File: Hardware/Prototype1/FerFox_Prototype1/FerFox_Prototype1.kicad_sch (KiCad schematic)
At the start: 33 parts, among them J1 Conn_01x08_Pin, J2 Conn_01x06_Pin, U1 STM32F401CCUx, Y1 25MHz, Y2 32768 Hz

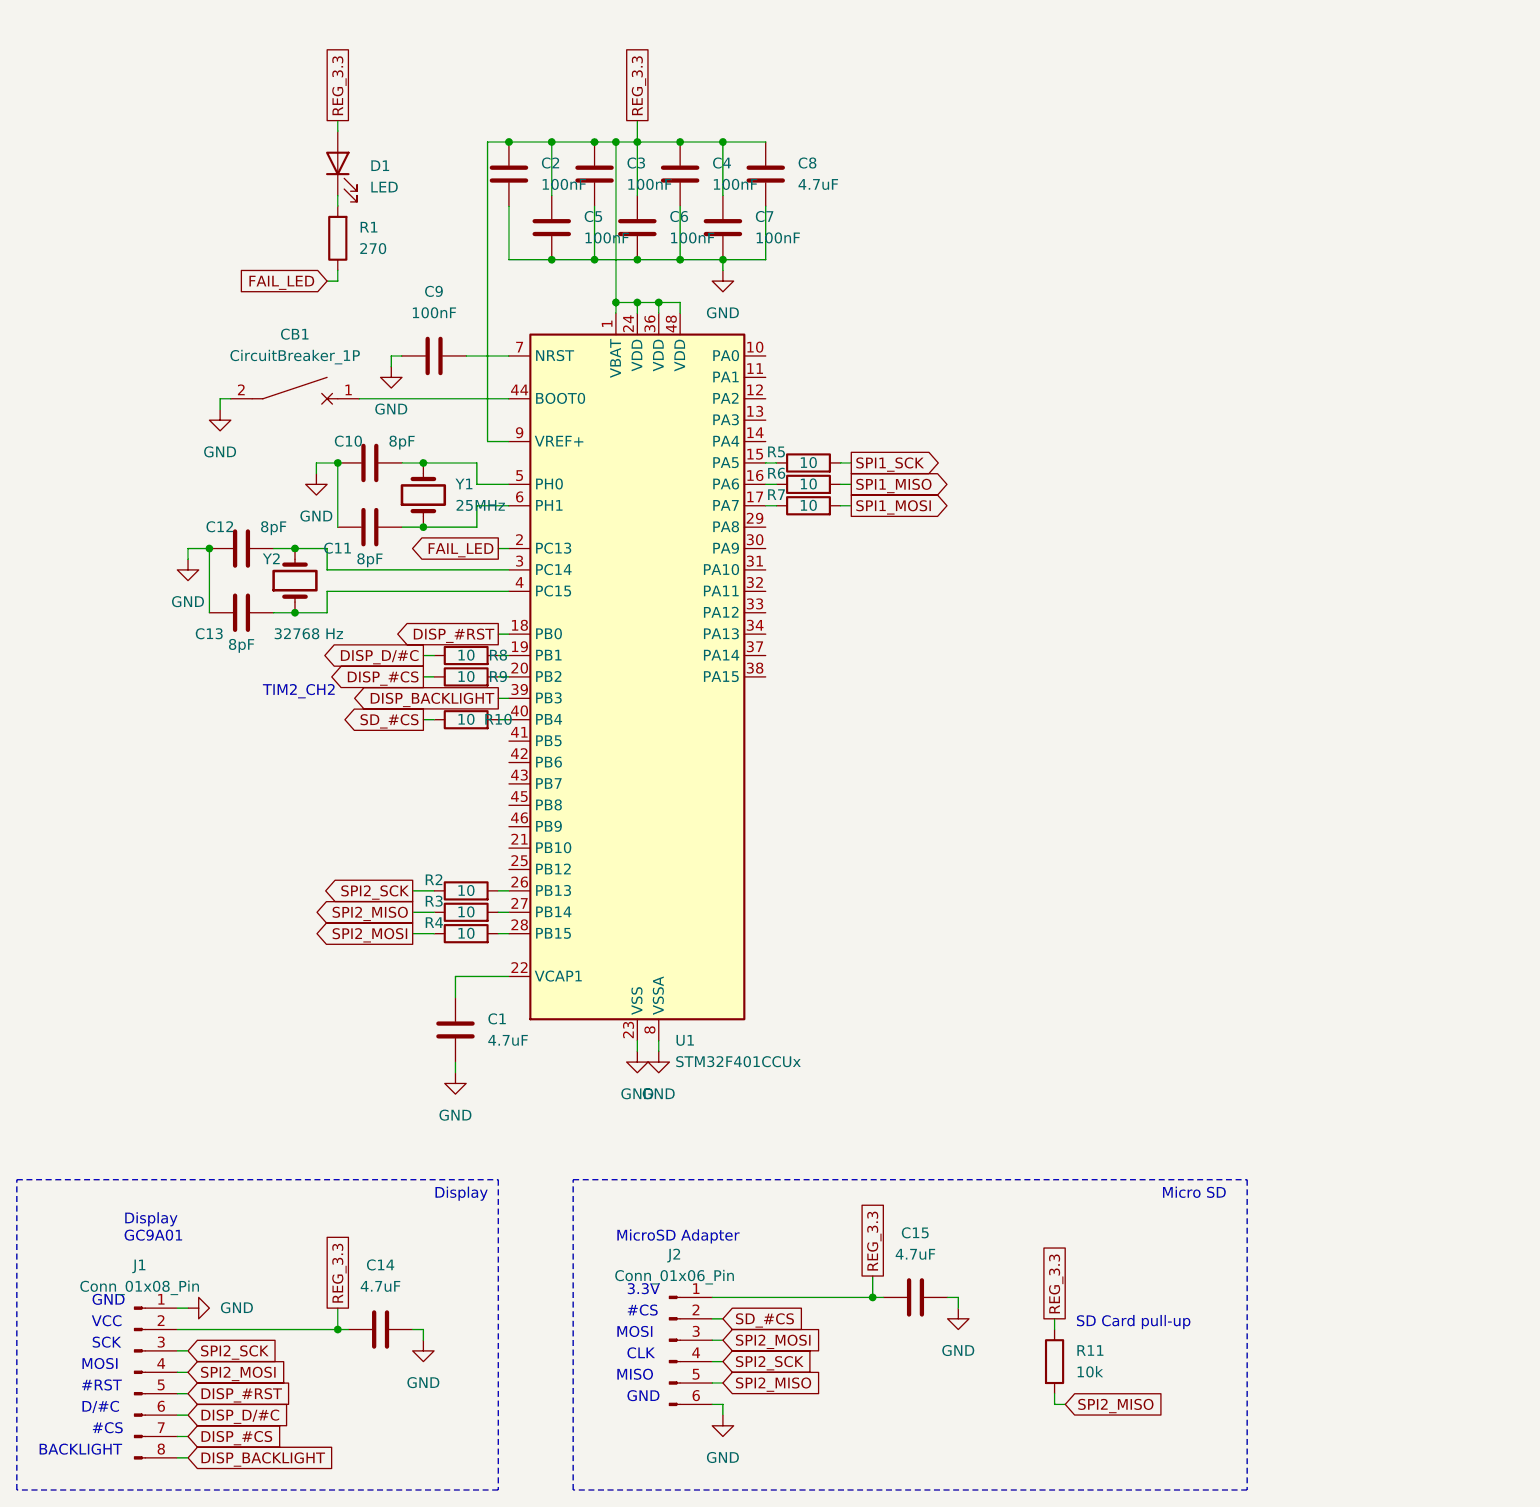
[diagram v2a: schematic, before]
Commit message: Added pSRAM to schematic
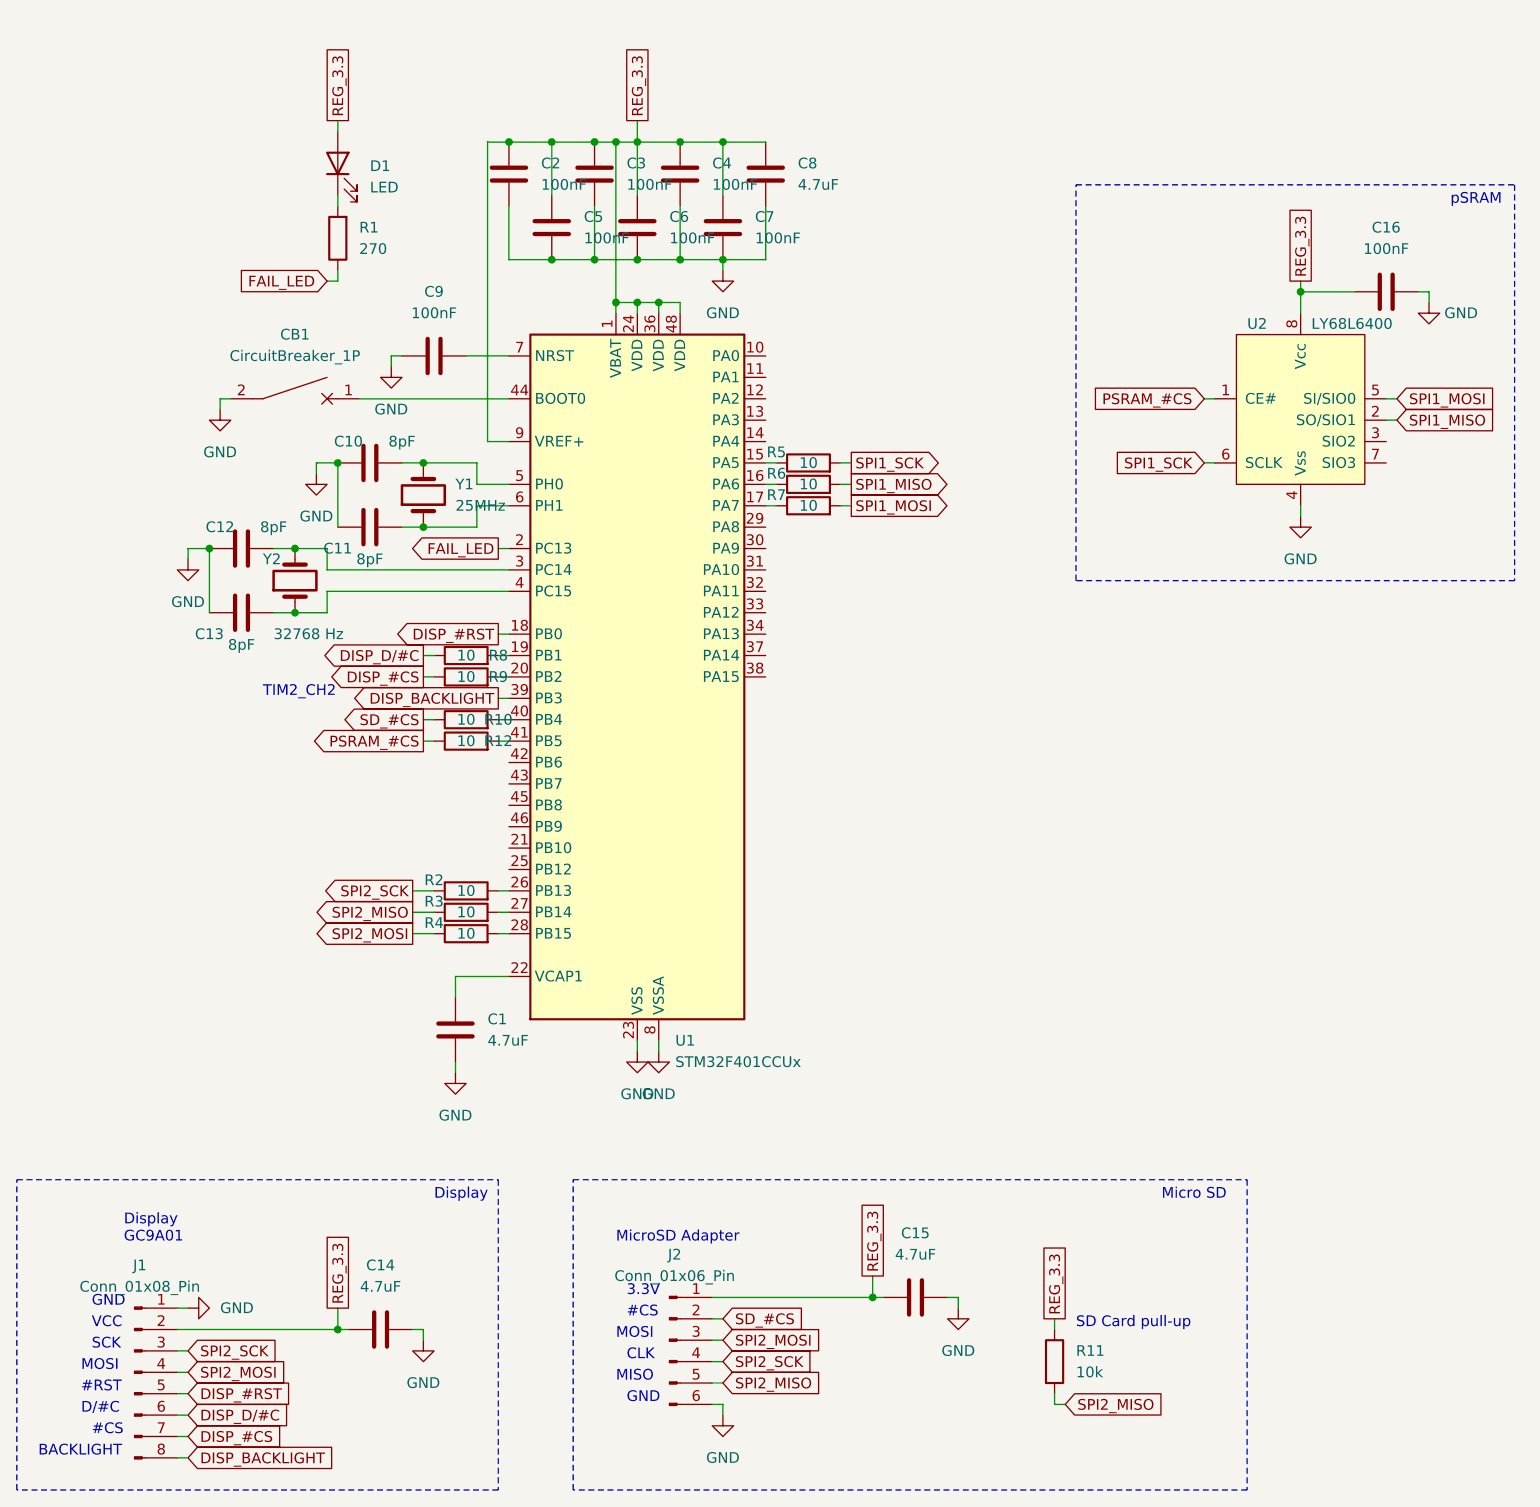
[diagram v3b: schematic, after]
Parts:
- added C16: 100nF, symbol Device:C
- added R12: 10, symbol Device:R
- added U2: LY68L6400, symbol fossa library:LY68L6400
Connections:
- net GND: now also C16.2, U2.4 (Vss)
- net REG_3.3: now also C16.1, U2.8 (Vcc)
- net SPI1_MISO: now also U2.2 (SO/SIO1)
- net SPI1_MOSI: now also U2.5 (SI/SIO0)
- net SPI1_SCK: now also U2.6 (SCLK)
- net at U1.41 (PB5): now also R12.2
- new net PSRAM_#CS: R12.1, U2.1 (CE#)
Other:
- note added: "pSRAM"
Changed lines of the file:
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@@
   (junction (at 231.14 49.53) (diameter 0) (color 0 0 0 0)
   )
+  (junction (at 299.72 53.34) (diameter 0) (color 0 0 0 0)
+  )
   (junction (at 195.58 73.66) (diameter 0) (color 0 0 0 0)
   )
@@
     (stroke (width 0) (type default))
   )
+  (wire (pts (xy 314.96 53.34) (xy 313.69 53.34))
+    (stroke (width 0) (type default))
+  )
   (wire (pts (xy 220.98 142.24) (xy 220.98 143.51))
     (stroke (width 0) (type default))
@@
     (stroke (width 0) (type default))
   )
+  (wire (pts (xy 195.58 106.68) (xy 196.85 106.68))
+    (stroke (width 0) (type default))
+  )
   (wire (pts (xy 185.42 52.07) (xy 185.42 50.8))
     (stroke (width 0) (type default))
@@
     (stroke (width 0) (type default))
   )
+  (wire (pts (xy 288.29 73.66) (xy 289.56 73.66))
+    (stroke (width 0) (type default))
+  )
+  (wire (pts (xy 299.72 52.07) (xy 299.72 53.34))
+    (stroke (width 0) (type default))
+  )
   (wire (pts (xy 205.74 76.2) (xy 201.93 76.2))
     (stroke (width 0) (type default))
@@
     (stroke (width 0) (type default))
   )
+  (wire (pts (xy 288.29 66.04) (xy 289.56 66.04))
+    (stroke (width 0) (type default))
+  )
   (wire (pts (xy 229.87 182.88) (xy 231.14 182.88))
     (stroke (width 0) (type default))
@@
     (stroke (width 0) (type default))
   )
+  (wire (pts (xy 299.72 53.34) (xy 299.72 55.88))
+    (stroke (width 0) (type default))
+  )
   (wire (pts (xy 226.06 49.53) (xy 231.14 49.53))
     (stroke (width 0) (type default))
@@
     (stroke (width 0) (type default))
   )
+  (wire (pts (xy 309.88 68.58) (xy 311.15 68.58))
+    (stroke (width 0) (type default))
+  )
   (wire (pts (xy 166.37 189.23) (xy 167.64 189.23))
     (stroke (width 0) (type default))
   )
+  (wire (pts (xy 299.72 78.74) (xy 299.72 80.01))
+    (stroke (width 0) (type default))
+  )
   (wire (pts (xy 194.31 129.54) (xy 196.85 129.54))
     (stroke (width 0) (type default))
@@
     (stroke (width 0) (type default))
   )
+  (wire (pts (xy 204.47 106.68) (xy 205.74 106.68))
+    (stroke (width 0) (type default))
+  )
   (wire (pts (xy 245.11 78.74) (xy 246.38 78.74))
     (stroke (width 0) (type default))
@@
     (stroke (width 0) (type default))
   )
+  (wire (pts (xy 309.88 66.04) (xy 311.15 66.04))
+    (stroke (width 0) (type default))
+  )
   (wire (pts (xy 270.51 185.42) (xy 271.78 185.42))
     (stroke (width 0) (type default))
@@
     (stroke (width 0) (type default))
   )
+  (wire (pts (xy 314.96 54.61) (xy 314.96 53.34))
+    (stroke (width 0) (type default))
+  )
   (wire (pts (xy 185.42 73.66) (xy 185.42 81.28))
     (stroke (width 0) (type default))
   )
+  (wire (pts (xy 299.72 53.34) (xy 306.07 53.34))
+    (stroke (width 0) (type default))
+  )
   (wire (pts (xy 195.58 176.53) (xy 194.31 176.53))
     (stroke (width 0) (type default))
@@
   (wire (pts (xy 194.31 124.46) (xy 196.85 124.46))
     (stroke (width 0) (type default))
+  )
+  (rectangle (start 273.05 40.64) (end 325.12 87.63)
+    (stroke (width 0) (type dash))
+    (fill (type none))
   )
   (rectangle (start 147.32 158.75) (end 204.47 195.58)
@@
   )
   (text "SCK" (at 156.21 179.07 0)
+    (effects (font (size 1.27 1.27)) (justify left bottom))
+  )
+  (text "pSRAM" (at 317.5 43.18 0)
     (effects (font (size 1.27 1.27)) (justify left bottom))
   )
@@
     )
   )
+  (global_label "REG_3.3" (shape passive) (at 299.72 52.07 90) (fields_autoplaced)
+    (effects (font (size 1.27 1.27)) (justify left))
+    (property "Intersheetrefs" "${INTERSHEET_REFS}" (at 299.72 42.5951 90)
+      (effects (font (size 1.27 1.27)) (justify left) hide)
+    )
+  )
+  (global_label "SPI1_MOSI" (shape input) (at 311.15 66.04 0) (fields_autoplaced)
+    (effects (font (size 1.27 1.27)) (justify left))
+    (property "Intersheetrefs" "${INTERSHEET_REFS}" (at 323.9928 66.04 0)
+      (effects (font (size 1.27 1.27)) (justify left) hide)
+    )
+  )
   (global_label "SPI2_MOSI" (shape output) (at 194.31 129.54 180) (fields_autoplaced)
     (effects (font (size 1.27 1.27)) (justify right))
@@
     )
   )
+  (global_label "SPI1_MISO" (shape input) (at 311.15 68.58 0) (fields_autoplaced)
+    (effects (font (size 1.27 1.27)) (justify left))
+    (property "Intersheetrefs" "${INTERSHEET_REFS}" (at 323.9928 68.58 0)
+      (effects (font (size 1.27 1.27)) (justify left) hide)
+    )
+  )
   (global_label "FAIL_LED" (shape input) (at 184.15 52.07 180) (fields_autoplaced)
     (effects (font (size 1.27 1.27)) (justify right))
@@
     )
   )
+  (global_label "PSRAM_#CS" (shape input) (at 288.29 66.04 180) (fields_autoplaced)
+    (effects (font (size 1.27 1.27)) (justify right))
+    (property "Intersheetrefs" "${INTERSHEET_REFS}" (at 274.2982 66.04 0)
+      (effects (font (size 1.27 1.27)) (justify right) hide)
+    )
+  )
+  (global_label "PSRAM_#CS" (shape output) (at 195.58 106.68 180) (fields_autoplaced)
+    (effects (font (size 1.27 1.27)) (justify right))
+    (property "Intersheetrefs" "${INTERSHEET_REFS}" (at 181.5882 106.68 0)
+      (effects (font (size 1.27 1.27)) (justify right) hide)
+    )
+  )
   (global_label "SPI2_SCK" (shape output) (at 194.31 124.46 180) (fields_autoplaced)
     (effects (font (size 1.27 1.27)) (justify right))
     (property "Intersheetrefs" "${INTERSHEET_REFS}" (at 182.3933 124.46 0)
+      (effects (font (size 1.27 1.27)) (justify right) hide)
+    )
+  )
+  (global_label "SPI1_SCK" (shape input) (at 288.29 73.66 180) (fields_autoplaced)
+    (effects (font (size 1.27 1.27)) (justify right))
+    (property "Intersheetrefs" "${INTERSHEET_REFS}" (at 276.2939 73.66 0)
       (effects (font (size 1.27 1.27)) (justify right) hide)
     )
@@
         (path "/011f2c64-cf22-44cd-a30f-ff566a75b03a"
           (reference "C11") (unit 1)
+        )
+      )
+    )
+  )
+  (symbol (lib_id "Device:C") (at 309.88 53.34 90) (unit 1)
+    (in_bom yes) (on_board yes) (dnp no) (fields_autoplaced)
+    (property "Reference" "C16" (at 309.88 45.72 90)
+      (effects (font (size 1.27 1.27)))
+    )
+    (property "Value" "100nF" (at 309.88 48.26 90)
+      (effects (font (size 1.27 1.27)))
+    )
+    (property "Footprint" "" (at 313.69 52.3748 0)
+      (effects (font (size 1.27 1.27)) hide)
+    )
+    (property "Datasheet" "~" (at 309.88 53.34 0)
+      (effects (font (size 1.27 1.27)) hide)
+    )
+    (pin "1")
+    (pin "2")
+    (instances
+      (project "FerFox_Prototype1"
+        (path "/011f2c64-cf22-44cd-a30f-ff566a75b03a"
+          (reference "C16") (unit 1)
         )
       )
@@
     )
   )
+  (symbol (lib_id "Device:R") (at 200.66 106.68 90) (unit 1)
+    (in_bom yes) (on_board yes) (dnp no)
+    (property "Reference" "R12" (at 204.47 106.68 90)
+      (effects (font (size 1.27 1.27)))
+    )
+    (property "Value" "10" (at 200.66 106.68 90)
+      (effects (font (size 1.27 1.27)))
+    )
+    (property "Footprint" "" (at 200.66 108.458 90)
+      (effects (font (size 1.27 1.27)) hide)
+    )
+    (property "Datasheet" "~" (at 200.66 106.68 0)
+      (effects (font (size 1.27 1.27)) hide)
+    )
+    (pin "1")
+    (pin "2")
+    (instances
+      (project "FerFox_Prototype1"
+        (path "/011f2c64-cf22-44cd-a30f-ff566a75b03a"
+          (reference "R12") (unit 1)
+        )
+      )
+    )
+  )
   (symbol (lib_id "power:GND") (at 231.14 50.8 0) (unit 1)
     (in_bom yes) (on_board yes) (dnp no) (fields_autoplaced)
@@
     )
   )
+  (symbol (lib_id "fossa library:LY68L6400") (at 299.72 53.34 0) (unit 1)
+    (in_bom yes) (on_board yes) (dnp no)
+    (property "Reference" "U2" (at 293.37 57.15 0)
+      (effects (font (size 1.27 1.27)) (justify left))
+    )
+    (property "Value" "LY68L6400" (at 300.99 57.15 0)
+      (effects (font (size 1.27 1.27)) (justify left))
+    )
+    (property "Footprint" "" (at 299.72 53.34 0)
+      (effects (font (size 1.27 1.27)) hide)
+    )
+    (property "Datasheet" "" (at 299.72 53.34 0)
+      (effects (font (size 1.27 1.27)) hide)
+    )
+    (pin "1")
+    (pin "2")
+    (pin "3")
+    (pin "4")
+    (pin "5")
+    (pin "6")
+    (pin "7")
+    (pin "8")
+    (instances
+      (project "FerFox_Prototype1"
+        (path "/011f2c64-cf22-44cd-a30f-ff566a75b03a"
+          (reference "U2") (unit 1)
+        )
+      )
+    )
+  )
   (symbol (lib_id "power:GND") (at 171.45 67.31 0) (unit 1)
     (in_bom yes) (on_board yes) (dnp no) (fields_autoplaced)
@@
         (path "/011f2c64-cf22-44cd-a30f-ff566a75b03a"
           (reference "C8") (unit 1)
+        )
+      )
+    )
+  )
+  (symbol (lib_id "power:GND") (at 314.96 54.61 0) (unit 1)
+    (in_bom yes) (on_board yes) (dnp no)
+    (property "Reference" "#PWR014" (at 314.96 60.96 0)
+      (effects (font (size 1.27 1.27)) hide)
+    )
+    (property "Value" "GND" (at 318.77 55.88 0)
+      (effects (font (size 1.27 1.27)))
+    )
+    (property "Footprint" "" (at 314.96 54.61 0)
+      (effects (font (size 1.27 1.27)) hide)
+    )
+    (property "Datasheet" "" (at 314.96 54.61 0)
+      (effects (font (size 1.27 1.27)) hide)
+    )
+    (pin "1")
+    (instances
+      (project "FerFox_Prototype1"
+        (path "/011f2c64-cf22-44cd-a30f-ff566a75b03a"
+          (reference "#PWR014") (unit 1)
         )
       )
@@
         )
       )
+    )
+  )
+  (symbol (lib_id "power:GND") (at 299.72 80.01 0) (unit 1)
+    (in_bom yes) (on_board yes) (dnp no) (fields_autoplaced)
+    (property "Reference" "#PWR013" (at 299.72 86.36 0)
+      (effects (font (size 1.27 1.27)) hide)
+    )
+    (property "Value" "GND" (at 299.72 85.09 0)
+      (effects (font (size 1.27 1.27)))
+    )
+    (property "Footprint" "" (at 299.72 80.01 0)
+      (effects (font (size 1.27 1.27)) hide)
+    )
+    (property "Datasheet" "" (at 299.72 80.01 0)
+      (effects (font (size 1.27 1.27)) hide)
+    )
+    (pin "1")
+    (instances
+      (project "FerFox_Prototype1"
+        (path "/011f2c64-cf22-44cd-a30f-ff566a75b03a"
+          (reference "#PWR013") (unit 1)
+        )
+      )
